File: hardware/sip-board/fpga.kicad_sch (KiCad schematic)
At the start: 2 parts, among them IC2 XC7S15-1CPGA196C

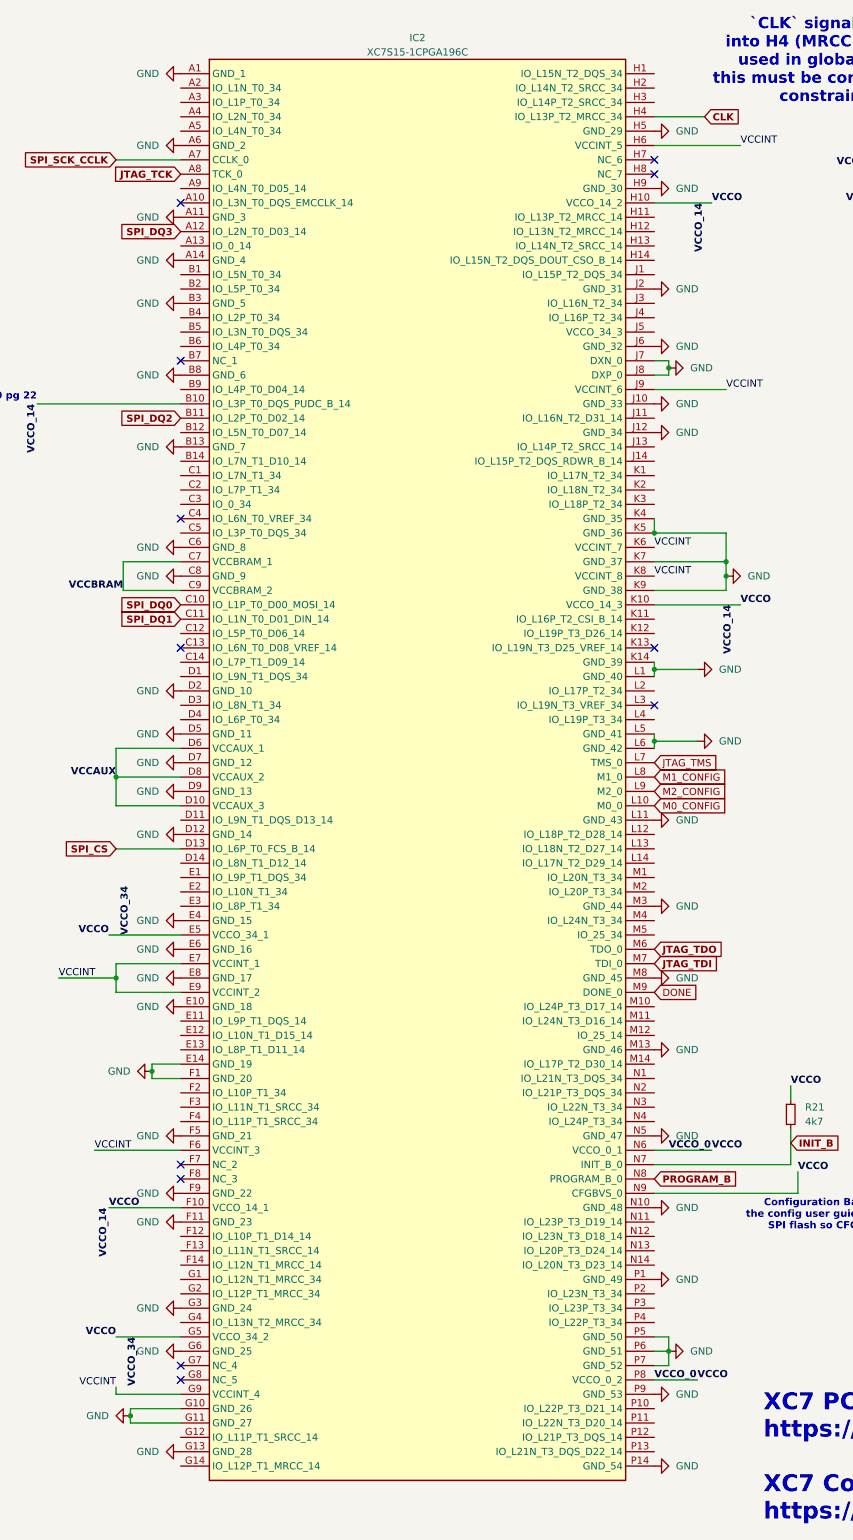
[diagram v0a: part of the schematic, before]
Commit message: routed to level shifters, need to address DRC
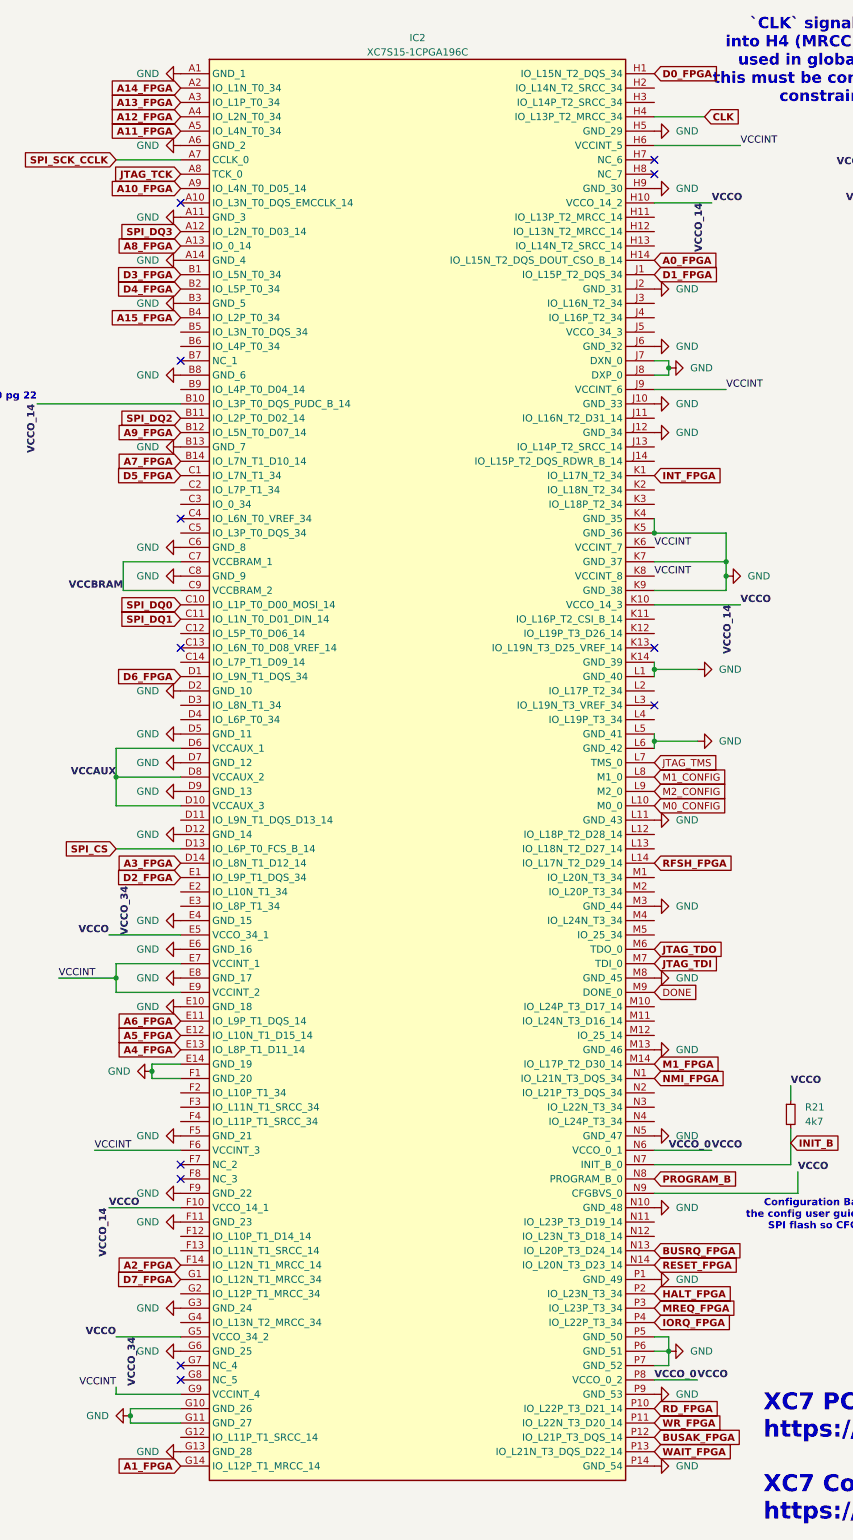
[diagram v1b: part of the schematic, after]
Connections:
- net A8_FPGA: now reaches IC2.A13 (IO_0_14)
- net A14_FPGA: now reaches IC2.A2 (IO_L1N_T0_34)
- net A13_FPGA: now reaches IC2.A3 (IO_L1P_T0_34)
- net A12_FPGA: now reaches IC2.A4 (IO_L2N_T0_34)
- net A11_FPGA: now reaches IC2.A5 (IO_L4N_T0_34)
- net A10_FPGA: now reaches IC2.A9 (IO_L4N_T0_D05_14)
- net D3_FPGA: now reaches IC2.B1 (IO_L5N_T0_34)
- net A9_FPGA: now reaches IC2.B12 (IO_L5N_T0_D07_14)
- net A7_FPGA: now reaches IC2.B14 (IO_L7N_T1_D10_14)
- net D4_FPGA: now reaches IC2.B2 (IO_L5P_T0_34)
- net A15_FPGA: now reaches IC2.B4 (IO_L2P_T0_34)
- net D5_FPGA: now reaches IC2.C1 (IO_L7N_T1_34)
- net D6_FPGA: now reaches IC2.D1 (IO_L9N_T1_DQS_34)
- net A3_FPGA: now reaches IC2.D14 (IO_L8N_T1_D12_14)
- net D2_FPGA: now reaches IC2.E1 (IO_L9P_T1_DQS_34)
- net A6_FPGA: now reaches IC2.E11 (IO_L9P_T1_DQS_14)
- net A5_FPGA: now reaches IC2.E12 (IO_L10N_T1_D15_14)
- net A4_FPGA: now reaches IC2.E13 (IO_L8P_T1_D11_14)
- net A2_FPGA: now reaches IC2.F14 (IO_L12N_T1_MRCC_14)
- net D7_FPGA: now reaches IC2.G1 (IO_L12N_T1_MRCC_34)
- net A1_FPGA: now reaches IC2.G14 (IO_L12P_T1_MRCC_14)
- net D0_FPGA: now reaches IC2.H1 (IO_L15N_T2_DQS_34)
- net A0_FPGA: now reaches IC2.H14 (IO_L15N_T2_DQS_DOUT_CSO_B_14)
- net D1_FPGA: now reaches IC2.J1 (IO_L15P_T2_DQS_34)
- net INT_FPGA: now reaches IC2.K1 (IO_L17N_T2_34)
- net RFSH_FPGA: now reaches IC2.L14 (IO_L17N_T2_D29_14)
- net M1_FPGA: now reaches IC2.M14 (IO_L17P_T2_D30_14)
- net NMI_FPGA: now reaches IC2.N1 (IO_L21N_T3_DQS_34)
- net BUSRQ_FPGA: now reaches IC2.N13 (IO_L20P_T3_D24_14)
- net RESET_FPGA: now reaches IC2.N14 (IO_L20N_T3_D23_14)
- net RD_FPGA: now reaches IC2.P10 (IO_L22P_T3_D21_14)
- net WR_FPGA: now reaches IC2.P11 (IO_L22N_T3_D20_14)
- net BUSAK_FPGA: now reaches IC2.P12 (IO_L21P_T3_DQS_14)
- net WAIT_FPGA: now reaches IC2.P13 (IO_L21N_T3_DQS_D22_14)
- net HALT_FPGA: now reaches IC2.P2 (IO_L23N_T3_34)
- net MREQ_FPGA: now reaches IC2.P3 (IO_L23P_T3_34)
- net IORQ_FPGA: now reaches IC2.P4 (IO_L22P_T3_34)
